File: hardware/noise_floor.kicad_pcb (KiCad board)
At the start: 2 copper layers, 51.5 x 56.6 mm, 10 parts, among them J1 In, J2 Out, J3 DC Power, J4 Edge/Effect Connector 1 (Edge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, J5 Edge/Effect Connector 2 (Edge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, J6 Edge/Node Connector 1 (Edge S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, J7 Edge/Node Connector 2 (Edge S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, J8 Edge/Node Connector 1 (Node S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, J9 Edge/Node Connector 2 (Node S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, SW1 Footswitch

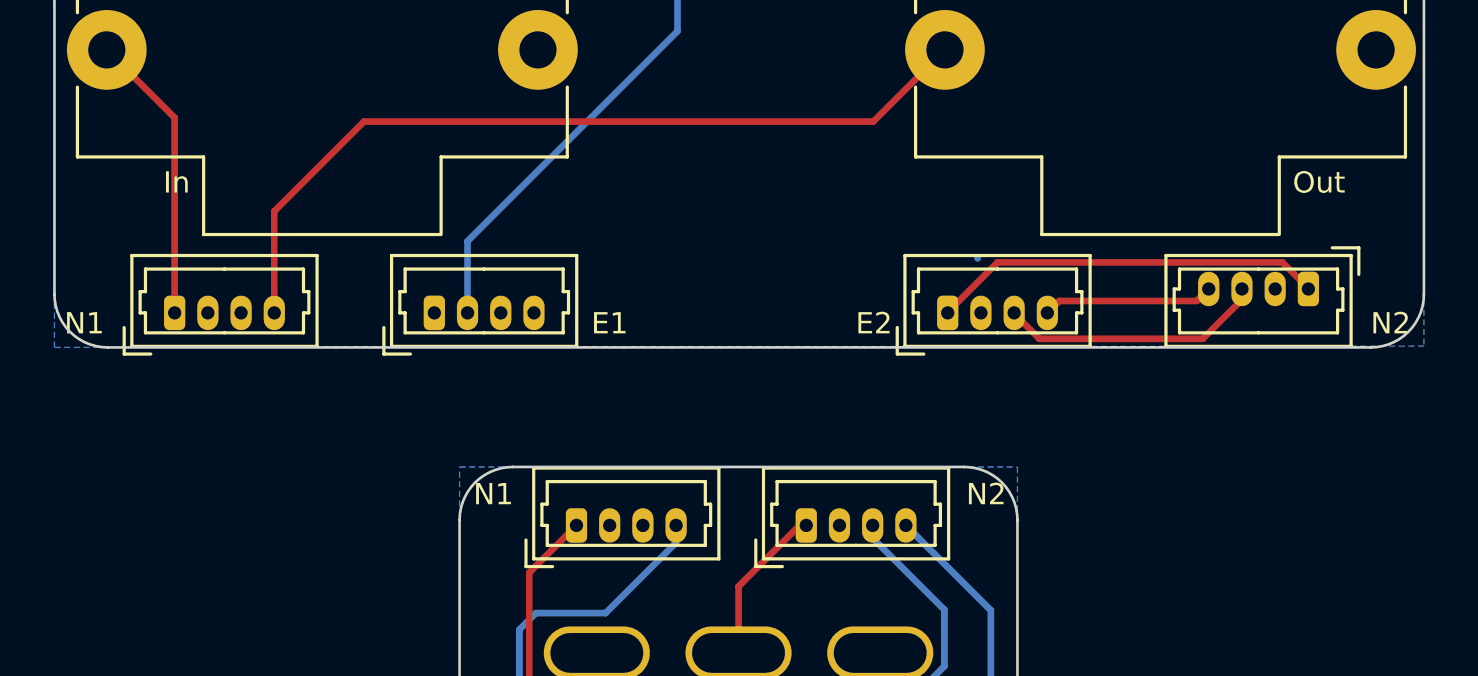
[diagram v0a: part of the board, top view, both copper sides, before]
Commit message: change name to Noise Floor
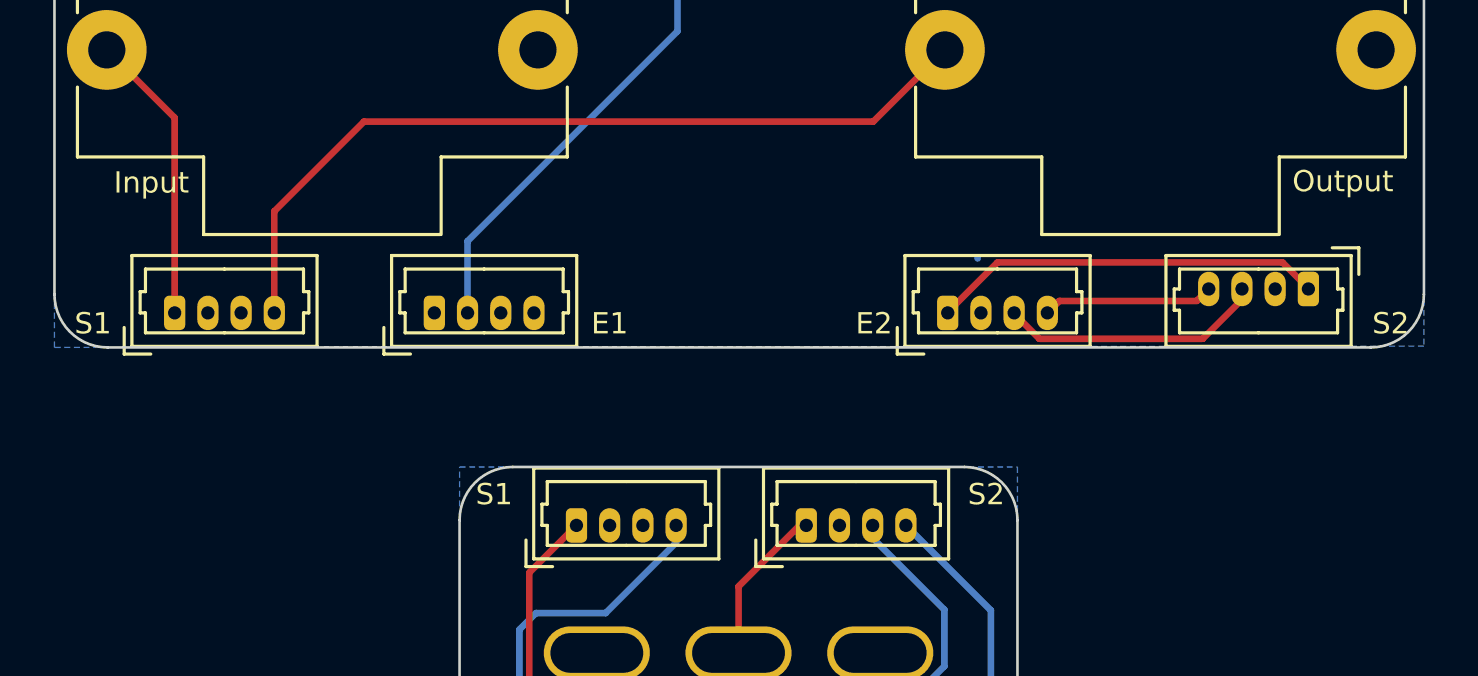
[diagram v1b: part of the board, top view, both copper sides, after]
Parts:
- J1: value In -> Input
- J2: value Out -> Output
- J4: value Edge/Effect Connector 1 (Edge Side) -> IO/Effect Connector 1 (IO Side)
- J5: value Edge/Effect Connector 2 (Edge Side) -> IO/Effect Connector 2 (IO Side)
- J6: value Edge/Node Connector 1 (Edge Side) -> IO/Switch Connector 1 (IO Side)
- J7: value Edge/Node Connector 2 (Edge Side) -> IO/Switch Connector 2 (IO Side)
- J8: value Edge/Node Connector 1 (Node Side) -> IO/Switch Connector 1 (Switch Side)
- J9: value Edge/Node Connector 2 (Node Side) -> IO/Switch Connector 2 (Switch Side)
- SW1: footprint attack_graph:SW_3PDT_SOLDER_LUGS -> noise_floor:SW_3PDT_SOLDER_LUGS
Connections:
- net /EFFECT_INPUT_EDGE renamed /EFFECT_INPUT_IO
- net /EFFECT_INPUT_NODE renamed /EFFECT_INPUT_SW
- net /EFFECT_OUTPUT_EDGE renamed /EFFECT_OUTPUT_IO
- net /EFFECT_OUTPUT_NODE renamed /EFFECT_OUTPUT_SW
- net /FS_EDGE renamed /FS_IO
- net /FS_NODE renamed /FS_SW
- net /GND_EDGE renamed /GND_IO
- net /GND_NODE renamed /GND_SW
- net /INPUT_TIP_EDGE renamed /INPUT_TIP_IO
- net /INPUT_TIP_NODE renamed /INPUT_TIP_SW
- net /OUTPUT_TIP_EDGE renamed /OUTPUT_TIP_IO
- net /OUTPUT_TIP_NODE renamed /OUTPUT_TIP_SW

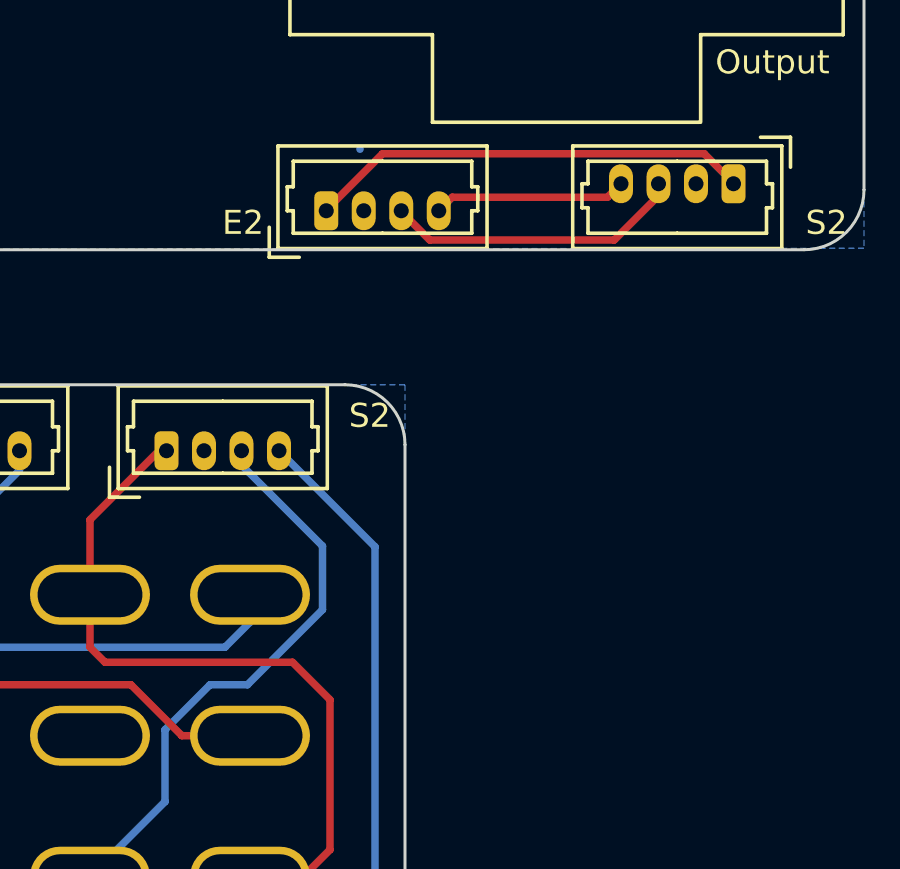
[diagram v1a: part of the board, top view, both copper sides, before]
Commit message: fix ordering of IO/Switch board connectors
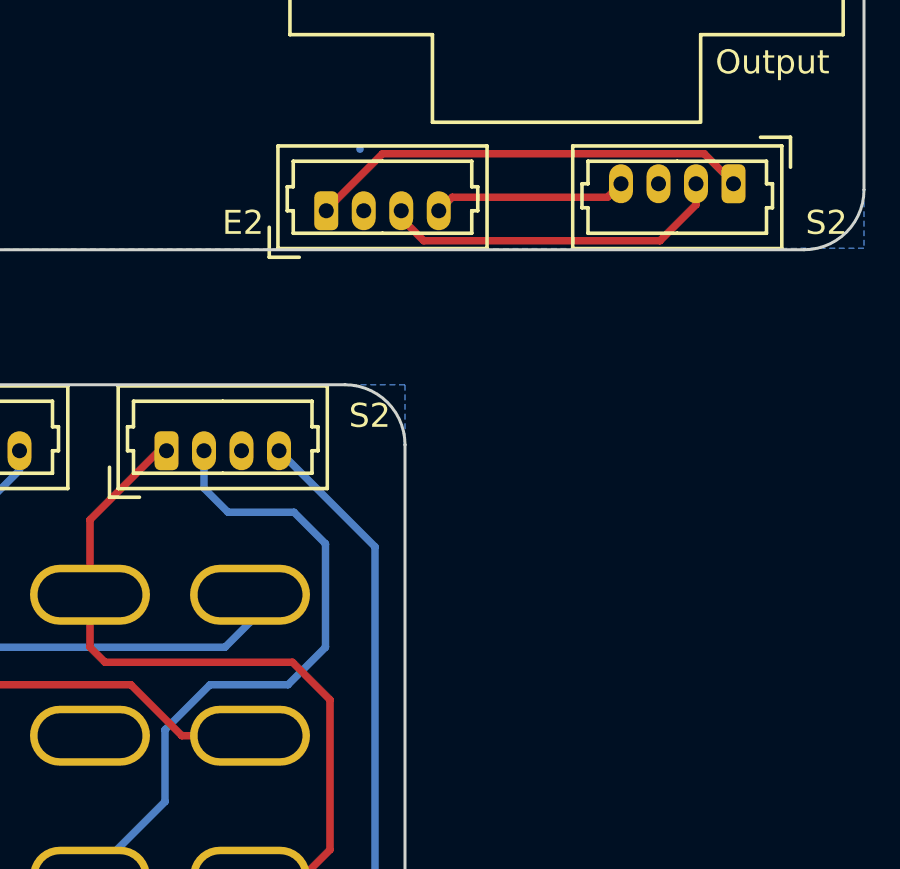
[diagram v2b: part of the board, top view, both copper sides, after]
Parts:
- J4: value IO/Effect Connector 1 (IO Side) -> IO/Effect Connector 1 (IO Side) [E1]
- J5: value IO/Effect Connector 2 (IO Side) -> IO/Effect Connector 2 (IO Side) [E2]
- J6: value IO/Switch Connector 1 (IO Side) -> IO/Switch Connector 1 (IO Side) [S1]
- J7: value IO/Switch Connector 2 (IO Side) -> IO/Switch Connector 2 (IO Side) [S2]
- J8: value IO/Switch Connector 1 (Switch Side) -> IO/Switch Connector 1 (Switch Side) [S1]
- J9: value IO/Switch Connector 2 (Switch Side) -> IO/Switch Connector 2 (Switch Side) [S2]
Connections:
- J7 pad 2: /GND_IO -> /FS_IO
- J7 pad 3: /FS_IO -> /GND_IO
- J9 pad 2: /GND_SW -> /FS_SW
- J9 pad 3: /FS_SW -> /GND_SW
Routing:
- net /FS_SW: track 19.3 -> 21.9 mm
- net /FS_IO: track 10.0 -> 11.6 mm
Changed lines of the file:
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@@
         (effects (font (size 1 1) (thickness 0.15)))
     )
-    (fp_text value "IO/Switch Connector 2 (IO Side)" (at 1.88 2.35) (layer "F.Fab")
+    (fp_text value "IO/Switch Connector 2 (IO Side) [S2]" (at 1.88 2.35) (layer "F.Fab")
         (effects (font (size 1 1) (thickness 0.15)))
     )
@@
       (net 6 "/EFFECT_INPUT_IO") (pinfunction "Pin_1") (pintype "passive"))
     (pad "2" thru_hole oval (at 1.25 0 180) (size 0.8 1.3) (drill 0.5) (layers "*.Cu" "*.Mask")
-      (net 3 "/GND_IO") (pinfunction "Pin_2") (pintype "passive"))
+      (net 7 "/FS_IO") (pinfunction "Pin_2") (pintype "passive"))
     (pad "3" thru_hole oval (at 2.5 0 180) (size 0.8 1.3) (drill 0.5) (layers "*.Cu" "*.Mask")
-      (net 7 "/FS_IO") (pinfunction "Pin_3") (pintype "passive"))
+      (net 3 "/GND_IO") (pinfunction "Pin_3") (pintype "passive"))
     (pad "4" thru_hole oval (at 3.75 0 180) (size 0.8 1.3) (drill 0.5) (layers "*.Cu" "*.Mask")
       (net 8 "/EFFECT_OUTPUT_IO") (pinfunction "Pin_4") (pintype "passive"))
@@
         (effects (font (size 1 1) (thickness 0.15)))
     )
-    (fp_text value "IO/Effect Connector 2 (IO Side)" (at 1.88 2.35) (layer "F.Fab")
+    (fp_text value "IO/Effect Connector 2 (IO Side) [E2]" (at 1.88 2.35) (layer "F.Fab")
         (effects (font (size 1 1) (thickness 0.15)))
     )
@@
         (effects (font (size 1 1) (thickness 0.15)))
     )
-    (fp_text value "IO/Effect Connector 1 (IO Side)" (at 1.88 2.35) (layer "F.Fab")
+    (fp_text value "IO/Effect Connector 1 (IO Side)  [E1]" (at 1.88 2.35) (layer "F.Fab")
         (effects (font (size 1 1) (thickness 0.15)))
     )
@@
         (effects (font (size 1 1) (thickness 0.15)))
     )
-    (fp_text value "IO/Switch Connector 1 (IO Side)" (at 1.88 2.35) (layer "F.Fab")
+    (fp_text value "IO/Switch Connector 1 (IO Side) [S1]" (at 1.88 2.35) (layer "F.Fab")
         (effects (font (size 1 1) (thickness 0.15)))
     )
@@
         (effects (font (size 1 1) (thickness 0.15)))
     )
-    (fp_text value "IO/Switch Connector 2 (Switch Side)" (at 1.88 2.35) (layer "F.Fab")
+    (fp_text value "IO/Switch Connector 2 (Switch Side) [S2]" (at 1.88 2.35) (layer "F.Fab")
         (effects (font (size 1 1) (thickness 0.15)))
     )
@@
       (net 11 "/EFFECT_INPUT_SW") (pinfunction "Pin_1") (pintype "passive"))
     (pad "2" thru_hole oval (at 1.25 0) (size 0.8 1.3) (drill 0.5) (layers "*.Cu" "*.Mask")
-      (net 12 "/GND_SW") (pinfunction "Pin_2") (pintype "passive"))
+      (net 13 "/FS_SW") (pinfunction "Pin_2") (pintype "passive"))
     (pad "3" thru_hole oval (at 2.5 0) (size 0.8 1.3) (drill 0.5) (layers "*.Cu" "*.Mask")
-      (net 13 "/FS_SW") (pinfunction "Pin_3") (pintype "passive"))
+      (net 12 "/GND_SW") (pinfunction "Pin_3") (pintype "passive"))
     (pad "4" thru_hole oval (at 3.75 0) (size 0.8 1.3) (drill 0.5) (layers "*.Cu" "*.Mask")
       (net 14 "/EFFECT_OUTPUT_SW") (pinfunction "Pin_4") (pintype "passive"))
@@
         (effects (font (size 1 1) (thickness 0.15)))
     )
-    (fp_text value "IO/Switch Connector 1 (Switch Side)" (at 1.88 2.35) (layer "F.Fab")
+    (fp_text value "IO/Switch Connector 1 (Switch Side) [S1]" (at 1.88 2.35) (layer "F.Fab")
         (effects (font (size 1 1) (thickness 0.15)))
     )
@@
   (segment (start 62.15 44.25) (end 62.15 44.224695) (width 0.25) (layer "F.Cu") (net 6))
   (segment (start 62.15 44.224695) (end 61.175305 43.25) (width 0.25) (layer "F.Cu") (net 6))
-  (segment (start 58.175 46.125) (end 52.024695 46.125) (width 0.25) (layer "F.Cu") (net 7))
-  (segment (start 59.65 44.65) (end 58.175 46.125) (width 0.25) (layer "F.Cu") (net 7))
-  (segment (start 59.65 44.25) (end 59.65 44.65) (width 0.25) (layer "F.Cu") (net 7))
-  (segment (start 52.024695 46.125) (end 51.075 45.175305) (width 0.25) (layer "F.Cu") (net 7))
-  (segment (start 51.075 45.175305) (end 51.075 45.15) (width 0.25) (layer "F.Cu") (net 7))
+  (segment (start 51.075 45.15) (end 51.075 45.4) (width 0.25) (layer "F.Cu") (net 7))
+  (segment (start 59.7 46.15) (end 60.9 44.95) (width 0.25) (layer "F.Cu") (net 7))
+  (segment (start 51.825 46.15) (end 59.7 46.15) (width 0.25) (layer "F.Cu") (net 7))
+  (segment (start 51.075 45.4) (end 51.825 46.15) (width 0.25) (layer "F.Cu") (net 7))
+  (segment (start 60.9 44.95) (end 60.9 44.25) (width 0.25) (layer "F.Cu") (net 7))
   (segment (start 58.4 44.25) (end 57.95 44.7) (width 0.25) (layer "F.Cu") (net 8))
   (segment (start 52.775 44.7) (end 52.325 45.15) (width 0.25) (layer "F.Cu") (net 8))
@@
   (segment (start 40.7 57.95) (end 40.7 55.45) (width 0.25) (layer "F.Cu") (net 11))
   (segment (start 40.7 59.7) (end 40.7 57.95) (width 0.25) (layer "F.Cu") (net 11))
-  (segment (start 48.45 56.325) (end 45.75 53.625) (width 0.25) (layer "B.Cu") (net 13))
-  (segment (start 48.45 58.45) (end 48.45 56.325) (width 0.25) (layer "B.Cu") (net 13))
-  (segment (start 45.95 60.95) (end 48.45 58.45) (width 0.25) (layer "B.Cu") (net 13))
-  (segment (start 44.7 60.95) (end 45.95 60.95) (width 0.25) (layer "B.Cu") (net 13))
+  (segment (start 45.75 53.625) (end 45.75 53.15) (width 0.25) (layer "B.Cu") (net 12))
+  (segment (start 44.7 60.95) (end 47.3 60.95) (width 0.25) (layer "B.Cu") (net 13))
+  (segment (start 40.7 67.348) (end 43.2 64.848) (width 0.25) (layer "B.Cu") (net 13))
   (segment (start 43.2 62.45) (end 44.7 60.95) (width 0.25) (layer "B.Cu") (net 13))
-  (segment (start 45.75 53.625) (end 45.75 53.15) (width 0.25) (layer "B.Cu") (net 13))
-  (segment (start 40.7 67.348) (end 43.2 64.848) (width 0.25) (layer "B.Cu") (net 13))
+  (segment (start 48.55 59.7) (end 48.55 56.25) (width 0.25) (layer "B.Cu") (net 13))
+  (segment (start 47.3 60.95) (end 48.55 59.7) (width 0.25) (layer "B.Cu") (net 13))
+  (segment (start 45.3 55.2) (end 44.5 54.4) (width 0.25) (layer "B.Cu") (net 13))
   (segment (start 43.2 64.848) (end 43.2 62.45) (width 0.25) (layer "B.Cu") (net 13))
+  (segment (start 44.5 54.4) (end 44.5 53.15) (width 0.25) (layer "B.Cu") (net 13))
+  (segment (start 47.5 55.2) (end 45.3 55.2) (width 0.25) (layer "B.Cu") (net 13))
+  (segment (start 48.55 56.25) (end 47.5 55.2) (width 0.25) (layer "B.Cu") (net 13))
   (segment (start 35.366 67.348) (end 35.366 68.366) (width 0.25) (layer "B.Cu") (net 14))
   (segment (start 48.7 69.95) (end 50.2 68.45) (width 0.25) (layer "B.Cu") (net 14))

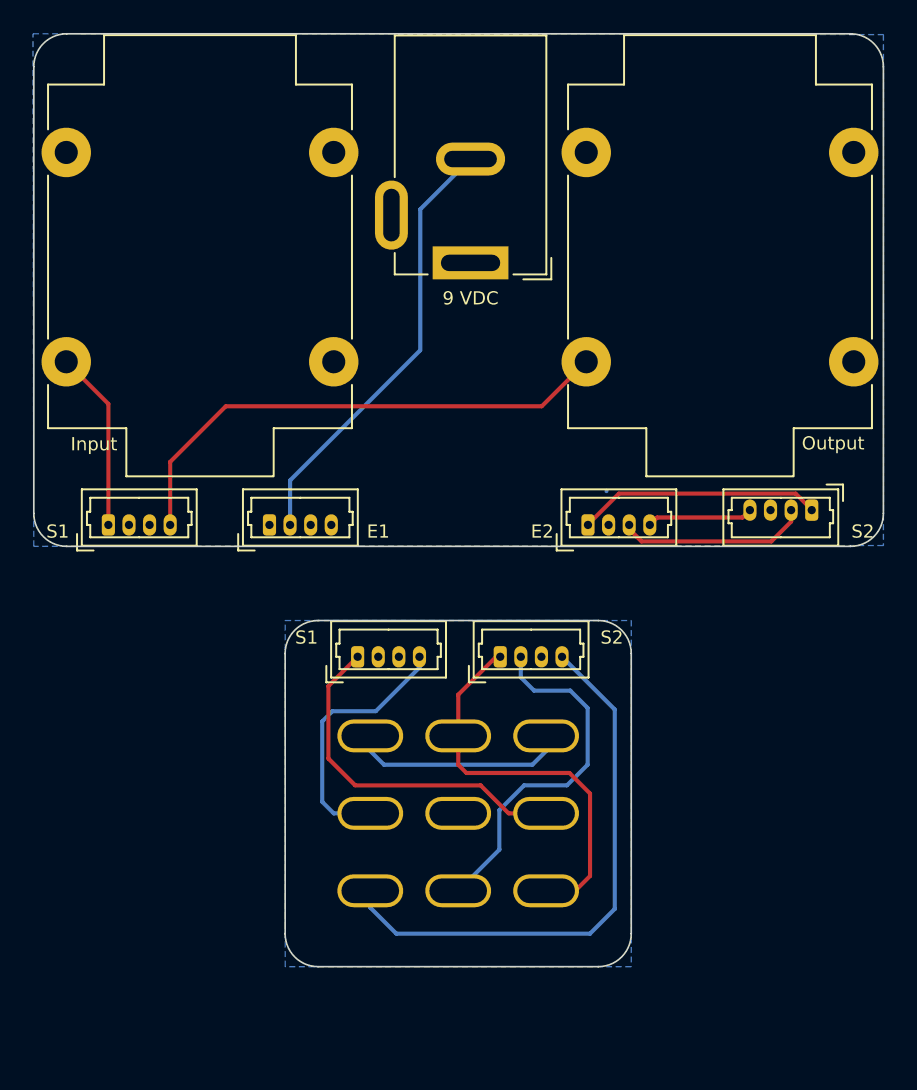
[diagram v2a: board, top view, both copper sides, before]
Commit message: Offload DC protection and LED indicator to "noise floor" utility boards
 - much rerouting and layout work, but functionally the same
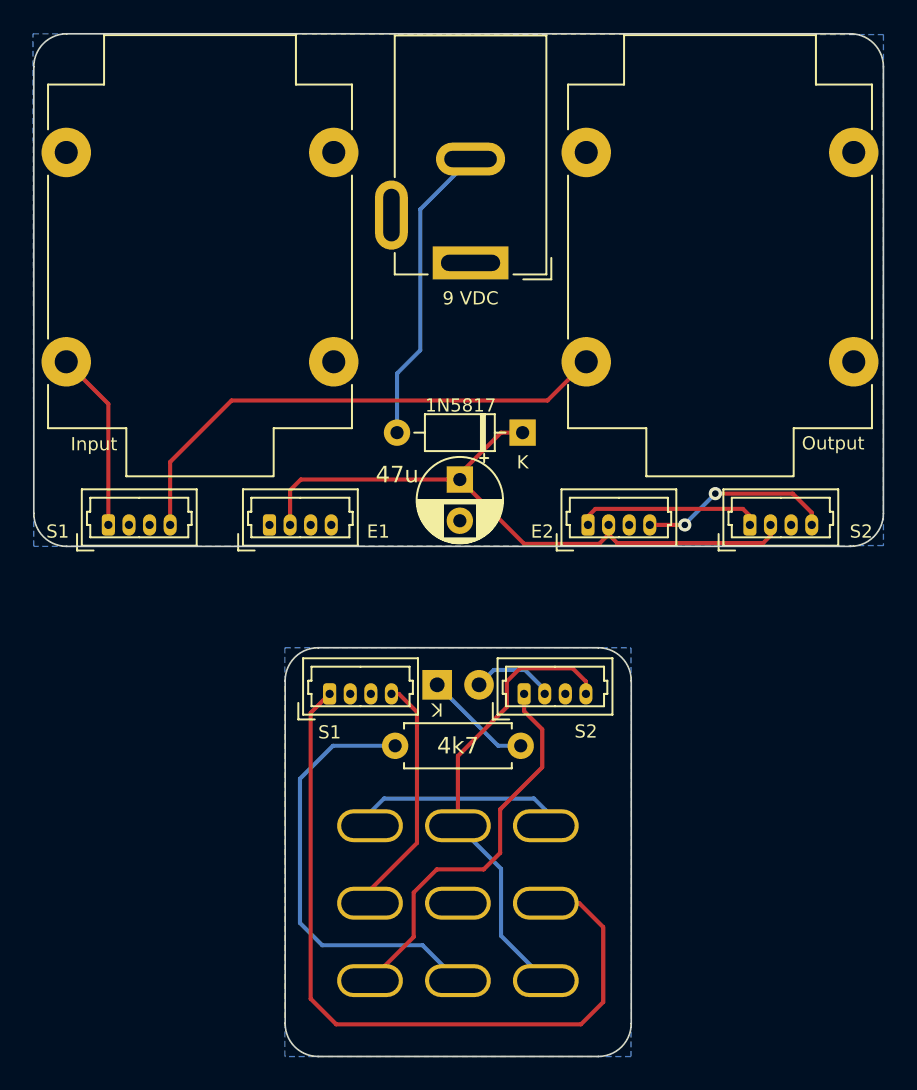
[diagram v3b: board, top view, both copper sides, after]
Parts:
- added C1: 47u, Capacitor_THT:CP_Radial_D5.0mm_P2.50mm, F.Cu at (40.8, 42.4)
- added D1: 1N5817, Diode_THT:D_DO-35_SOD27_P7.62mm_Horizontal, F.Cu at (44.6, 39.5)
- added D2: On, LED_THT:LED_D3.0mm, B.Cu at (39.4, 54.9)
- added R1: 4k7, Resistor_THT:R_Axial_DIN0207_L6.3mm_D2.5mm_P7.62mm_Horizontal, F.Cu at (44.5, 58.5)
- moved SW1 5.45 mm to (40.7, 68.1)
- moved J7 3.86 mm to (58.4, 45.1), turned to 0 degrees
- moved J8 2.82 mm to (32.9, 55.4)
- moved J9 2.68 mm to (44.7, 55.4)
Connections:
- J1 pad S: /GND_IO -> GND
- J2 pad S: /GND_IO -> GND
- J3 pad 1: /GND_IO -> GND
- J4 pad 2: /DC_SHIELD -> /9V0_IO
- J5 pad 1: /EFFECT_INPUT_IO -> /EFFECT_OUTPUT_IO
- J5 pad 2: /GND_IO -> /9V0_IO
- J5 pad 3: /FS_IO -> GND
- J5 pad 4: /EFFECT_OUTPUT_IO -> /EFFECT_INPUT_IO
- J7 pad 1: /EFFECT_INPUT_IO -> /EFFECT_OUTPUT_IO
- J7 pad 2: /FS_IO -> /9V0_IO
- J7 pad 3: /GND_IO -> GND
- J7 pad 4: /EFFECT_OUTPUT_IO -> /EFFECT_INPUT_IO
- J9 pad 1: /EFFECT_INPUT_SW -> /EFFECT_OUTPUT_SW
- J9 pad 2: /FS_SW -> /9V0_SW
- J9 pad 4: /EFFECT_OUTPUT_SW -> /EFFECT_INPUT_SW
- SW1 pad 6: /FS_SW -> Net-(SW1B-B3)
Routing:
- net /9V0_IO: track 0.00 -> 40.2 mm
- net Net-(SW1B-B3): track 0.00 -> 26.4 mm
- net /INPUT_TIP_SW: track 21.5 -> 46.6 mm
- net /FS_SW: track 21.9 -> 0.00 mm
- net /FS_IO: track 11.6 -> 0.00 mm
- net /EFFECT_OUTPUT_SW: track 33.8 -> 23.9 mm
- net /DC_SHIELD: track 26.7 -> 18.4 mm
- net Net-(D2-K): track 0.00 -> 6.60 mm
- net /9V0_SW: track 0.00 -> 5.10 mm
- net /EFFECT_OUTPUT_IO: track 6.45 -> 11.3 mm
- net /EFFECT_INPUT_SW: track 24.5 -> 27.8 mm
- net /EFFECT_INPUT_IO: track 14.8 -> 11.9 mm, vias 0 -> 2
- net /OUTPUT_TIP_SW: track 16.0 -> 14.8 mm
- added copper zone on B.Cu, net GND
- removed copper zone on B.Cu, net /GND_IO
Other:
- board size 51.5 x 56.6 mm -> 51.5 x 62.1 mm
